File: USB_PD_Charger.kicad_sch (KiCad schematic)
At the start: 42 parts, among them J9 Conn_01x05, Q1 AON7403, Q5 2N7002W, Q6 2N7002W, Q7 2N7002W, U1 LM3489MMX/NOPB, U2 TPS65987DDHRSHR, U3 MX25L8006EM1I-12G

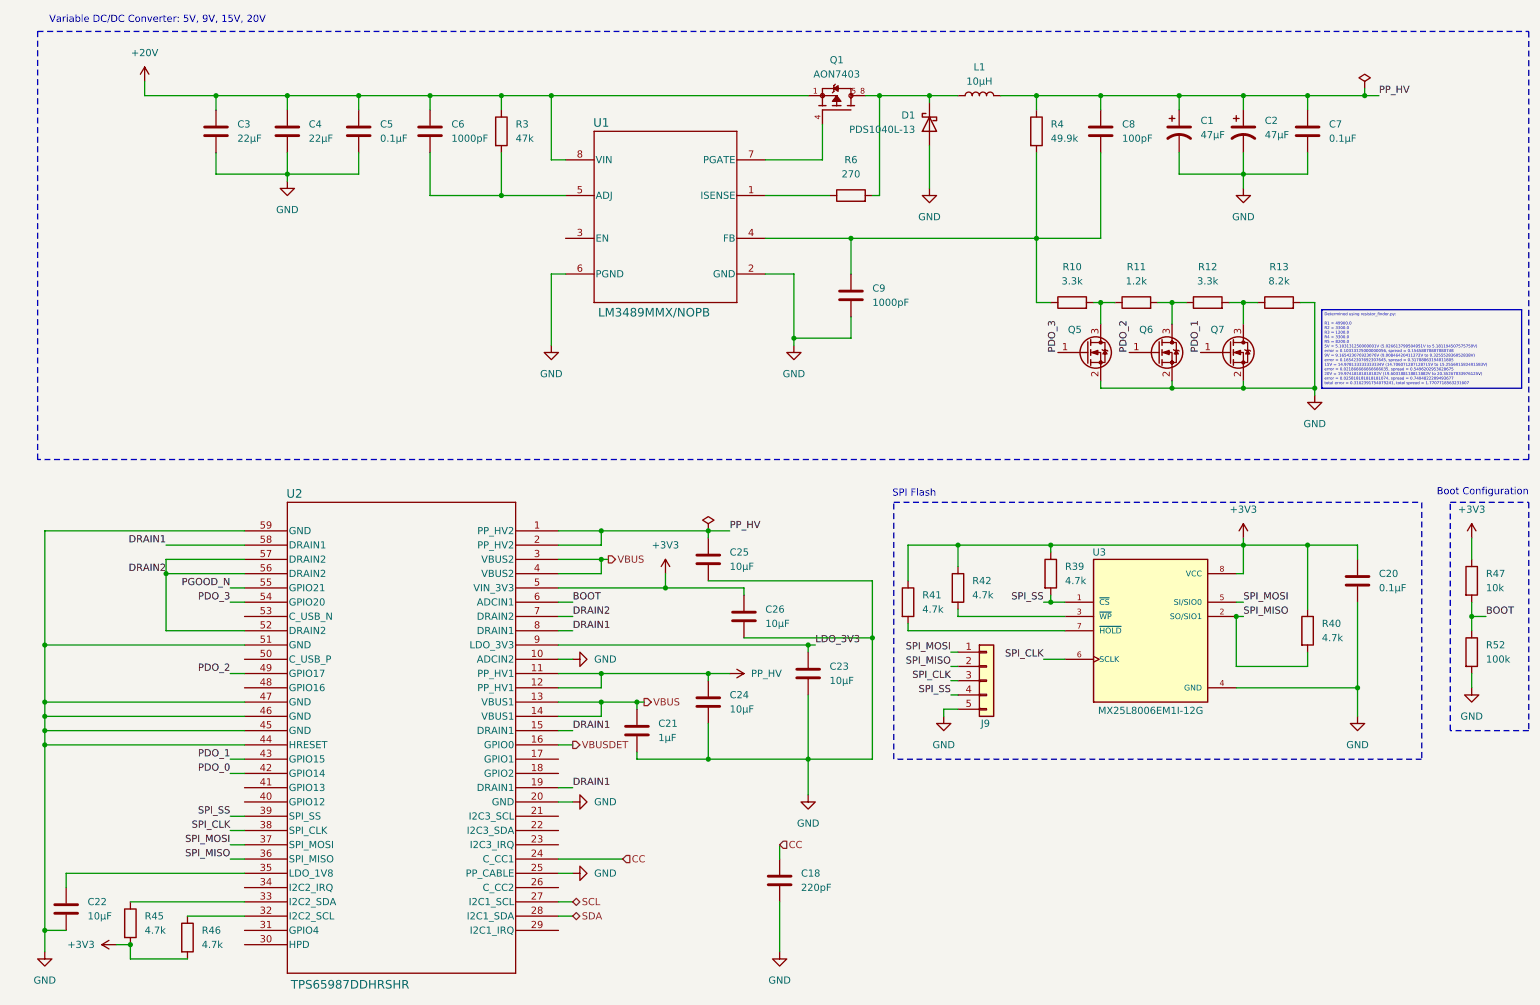
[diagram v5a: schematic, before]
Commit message: Ensure SPI flash is powered on even when board loses power
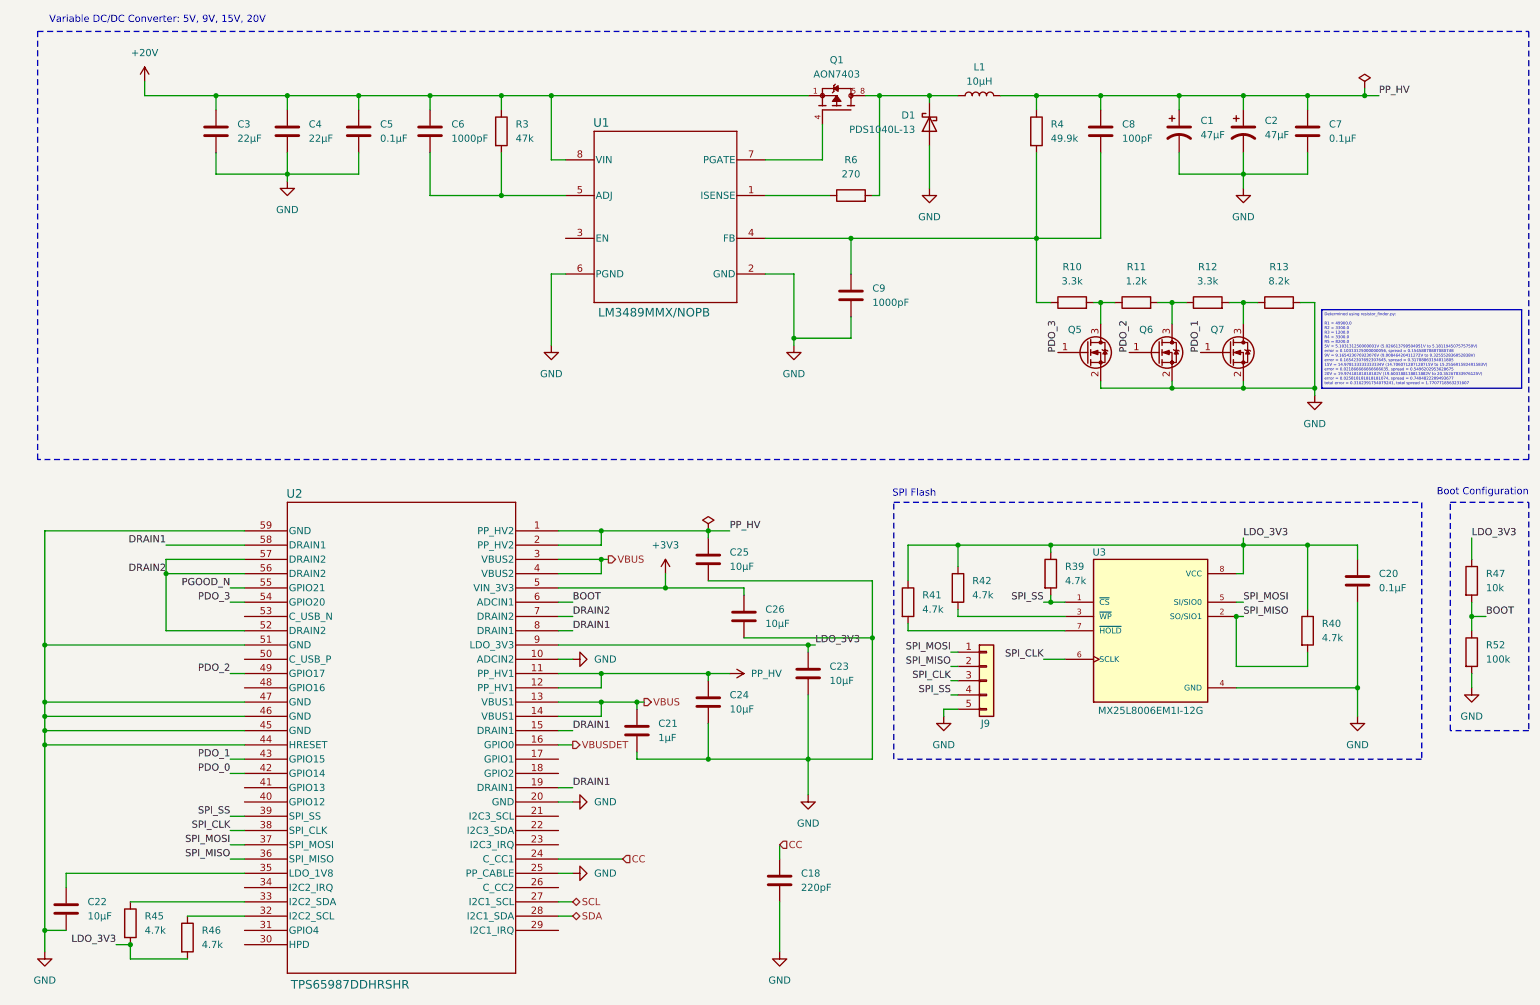
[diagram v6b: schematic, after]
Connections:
- net +3V3: no longer C20.1, R39.1, R40.1, R41.1, R42.1, R45.2, R46.2, R47.1, U3.8 (VCC)
- net LDO_3V3: now also C20.1, R39.1, R40.1, R41.1, R42.1, R45.2, R46.2, R47.1, U3.8 (VCC)
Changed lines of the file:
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@@
 		)
 	)
+	(label "LDO_3V3"
+		(at 231.14 111.76 0)
+		(fields_autoplaced yes)
+		(effects
+			(font
+				(size 1.27 1.27)
+			)
+			(justify left bottom)
+		)
+	)
 	(label "SPI_SS"
 		(at 50.8 161.29 180)
@@
 	)
 	(label "LDO_3V3"
+		(at 271.78 111.76 0)
+		(fields_autoplaced yes)
+		(effects
+			(font
+				(size 1.27 1.27)
+			)
+			(justify left bottom)
+		)
+	)
+	(label "LDO_3V3"
 		(at 154.94 130.81 0)
 		(fields_autoplaced yes)
@@
 		)
 	)
+	(label "LDO_3V3"
+		(at 30.48 184.15 180)
+		(fields_autoplaced yes)
+		(effects
+			(font
+				(size 1.27 1.27)
+			)
+			(justify right bottom)
+		)
+	)
 	(label "DRAIN2"
 		(at 111.76 125.73 0)
@@
 	)
 	(symbol
-		(lib_id "power:+3V3")
-		(at 231.14 111.76 0)
-		(unit 1)
-		(exclude_from_sim no)
-		(in_bom yes)
-		(on_board yes)
-		(dnp no)
-		(fields_autoplaced yes)
-		(property "Reference" "#PWR02"
-			(at 231.14 115.57 0)
-			(effects
-				(font
-					(size 1.27 1.27)
-				)
-				(hide yes)
-			)
-		)
-		(property "Value" "+3V3"
-			(at 231.14 106.68 0)
-			(effects
-				(font
-					(size 1.27 1.27)
-				)
-			)
-		)
-		(property "Footprint" ""
-			(at 231.14 111.76 0)
-			(effects
-				(font
-					(size 1.27 1.27)
-				)
-				(hide yes)
-			)
-		)
-		(property "Datasheet" ""
-			(at 231.14 111.76 0)
-			(effects
-				(font
-					(size 1.27 1.27)
-				)
-				(hide yes)
-			)
-		)
-		(property "Description" "Power symbol creates a global label with name \"+3V3\""
-			(at 231.14 111.76 0)
-			(effects
-				(font
-					(size 1.27 1.27)
-				)
-				(hide yes)
-			)
-		)
-		(pin "1"
-		)
-		(instances
-			(project "XG_Mobile_Dock"
-				(path "/f97e6956-ab08-42cb-8fed-03fa58e87f0e/fa35204a-fbf7-48de-bc5b-11fc2e29f675"
-					(reference "#PWR02")
-					(unit 1)
-				)
-			)
-		)
-	)
-	(symbol
 		(lib_id "Device:C")
 		(at 205.74 39.37 0)
@@
 					(unit 1)
 				)
-			)
-		)
-	)
-	(symbol
-		(lib_id "power:+3V3")
-		(at 30.48 184.15 90)
-		(unit 1)
-		(exclude_from_sim no)
-		(in_bom yes)
-		(on_board yes)
-		(dnp no)
-		(fields_autoplaced yes)
-		(property "Reference" "#PWR010"
-			(at 34.29 184.15 0)
-			(effects
-				(font
-					(size 1.27 1.27)
-				)
-				(hide yes)
-			)
-		)
-		(property "Value" "+3V3"
-			(at 26.67 184.1499 90)
-			(effects
-				(font
-					(size 1.27 1.27)
-				)
-				(justify left)
-			)
-		)
-		(property "Footprint" ""
-			(at 30.48 184.15 0)
-			(effects
-				(font
-					(size 1.27 1.27)
-				)
-				(hide yes)
-			)
-		)
-		(property "Datasheet" ""
-			(at 30.48 184.15 0)
-			(effects
-				(font
-					(size 1.27 1.27)
-				)
-				(hide yes)
-			)
-		)
-		(property "Description" "Power symbol creates a global label with name \"+3V3\""
-			(at 30.48 184.15 0)
-			(effects
-				(font
-					(size 1.27 1.27)
-				)
-				(hide yes)
-			)
-		)
-		(pin "1"
-		)
-		(instances
-			(project "XG_Mobile_Dock"
-				(path "/f97e6956-ab08-42cb-8fed-03fa58e87f0e/fa35204a-fbf7-48de-bc5b-11fc2e29f675"
-					(reference "#PWR010")
-					(unit 1)
-				)
-			)
-		)
-	)
-	(symbol
-		(lib_id "power:+3V3")
-		(at 271.78 111.76 0)
-		(unit 1)
-		(exclude_from_sim no)
-		(in_bom yes)
-		(on_board yes)
-		(dnp no)
-		(fields_autoplaced yes)
-		(property "Reference" "#PWR015"
-			(at 271.78 115.57 0)
-			(effects
-				(font
-					(size 1.27 1.27)
-				)
-				(hide yes)
-			)
-		)
-		(property "Value" "+3V3"
-			(at 271.78 106.68 0)
-			(effects
-				(font
-					(size 1.27 1.27)
-				)
-			)
-		)
-		(property "Footprint" ""
-			(at 271.78 111.76 0)
-			(effects
-				(font
-					(size 1.27 1.27)
-				)
-				(hide yes)
-			)
-		)
-		(property "Datasheet" ""
-			(at 271.78 111.76 0)
-			(effects
-				(font
-					(size 1.27 1.27)
-				)
-				(hide yes)
-			)
-		)
-		(property "Description" "Power symbol creates a global label with name \"+3V3\""
-			(at 271.78 111.76 0)
-			(effects
-				(font
-					(size 1.27 1.27)
-				)
-				(hide yes)
-			)
-		)
-		(pin "1"
-		)
-		(instances
-			(project "XG_Mobile_Dock"
-				(path "/f97e6956-ab08-42cb-8fed-03fa58e87f0e/fa35204a-fbf7-48de-bc5b-11fc2e29f675"
-					(reference "#PWR015")
-					(unit 1)
-				)

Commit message: pcb: fixed wrong voltage decoupling capacitor for PP_HV
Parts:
- C24, C25: footprint Capacitor_SMD:C_0402_1005Metric -> Capacitor_SMD:C_0603_1608Metric; LCSC C15525 -> C96446; Part_Number CL05A106MQ5NUNC -> CL10A106MA8NRNC
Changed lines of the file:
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@@
 			)
 		)
-		(property "Footprint" "Capacitor_SMD:C_0402_1005Metric"
+		(property "Footprint" "Capacitor_SMD:C_0603_1608Metric"
 			(at 136.8552 144.78 0)
 			(effects
@@
 			)
 		)
-		(property "Part_Number" "CL05A106MQ5NUNC"
+		(property "Part_Number" "CL10A106MA8NRNC"
 			(at 135.89 140.97 0)
 			(effects
@@
 			)
 		)
-		(property "LCSC" "C15525"
+		(property "LCSC" "C96446"
 			(at 135.89 140.97 0)
 			(effects
@@
 			)
 		)
-		(property "Footprint" "Capacitor_SMD:C_0402_1005Metric"
+		(property "Footprint" "Capacitor_SMD:C_0603_1608Metric"
 			(at 136.8552 119.38 0)
 			(effects
@@
 			)
 		)
-		(property "Part_Number" "CL05A106MQ5NUNC"
+		(property "Part_Number" "CL10A106MA8NRNC"
 			(at 135.89 115.57 0)
 			(effects
@@
 			)
 		)
-		(property "LCSC" "C15525"
+		(property "LCSC" "C96446"
 			(at 135.89 115.57 0)
 			(effects
